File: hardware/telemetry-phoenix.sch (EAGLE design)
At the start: 111 parts, among them IC10 TPS70933, IC11 VN5160S-E, IC2 TPS70933, IC3 BME280, IC4 STM32L052C8T6, IC5 TPS62160, IC6 HX1, IC7 LMP7702, IC8 ADXL345, IC9 VN5160S-E, J1 GPS1, J2 RASPBERRYPI-GPIO, J3 POWER, J4 GPS2, J5 DNP, J6 SMA_EDGE, J9 IO, Q1 SI4202DY, Y1 32768, Y2 8M

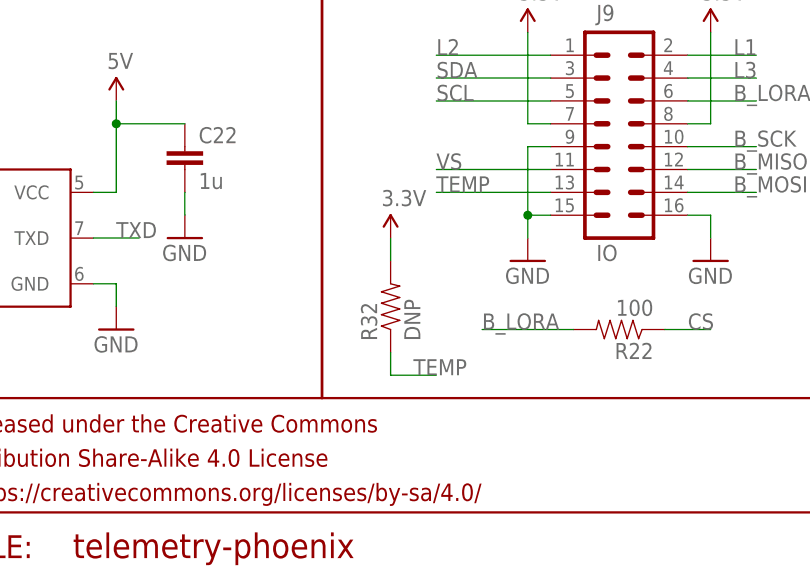
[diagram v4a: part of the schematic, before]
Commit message: Satisfy Adi on Phoenix power supply routing
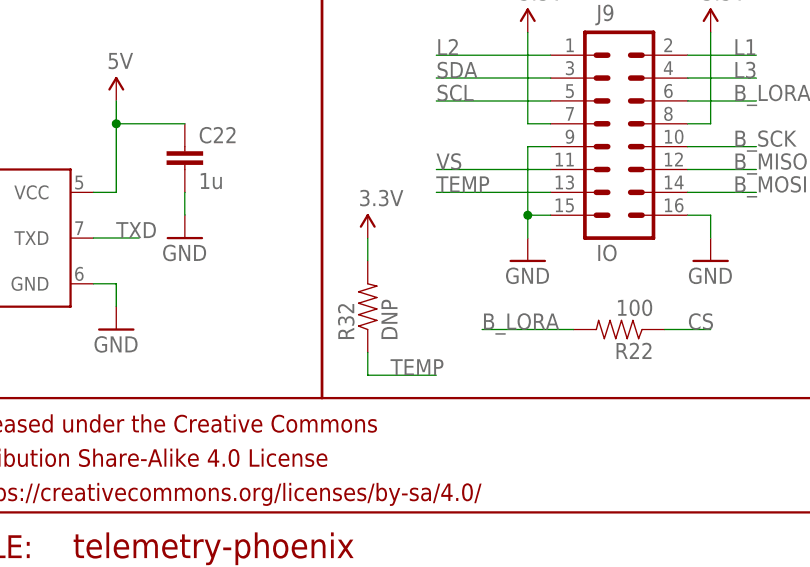
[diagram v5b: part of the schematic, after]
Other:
- moved on the sheet: R32
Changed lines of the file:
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@@
 <attribute name="VALUE" x="106.68" y="23.0886" size="1.778" layer="96"/>
 </instance>
-<instance part="R32" gate="G$1" x="198.12" y="45.72" rot="R90"/>
-<instance part="SUPPLY20" gate="G$1" x="198.12" y="53.34"/>
+<instance part="R32" gate="G$1" x="195.58" y="45.72" rot="R90"/>
+<instance part="SUPPLY20" gate="G$1" x="195.58" y="53.34"/>
 <instance part="R4" gate="G$1" x="368.3" y="137.16" rot="R180"/>
 <instance part="R25" gate="G$1" x="368.3" y="129.54" rot="R180"/>
@@
 <pinref part="R32" gate="G$1" pin="2"/>
 <pinref part="SUPPLY20" gate="G$1" pin="3.3V"/>
-<wire x1="198.12" y1="53.34" x2="198.12" y2="50.8" width="0.1524" layer="91"/>
+<wire x1="195.58" y1="53.34" x2="195.58" y2="50.8" width="0.1524" layer="91"/>
 </segment>
 <segment>
@@
 <segment>
 <pinref part="R32" gate="G$1" pin="1"/>
-<wire x1="198.12" y1="40.64" x2="198.12" y2="38.1" width="0.1524" layer="91"/>
-<wire x1="198.12" y1="38.1" x2="203.2" y2="38.1" width="0.1524" layer="91"/>
-<label x="200.66" y="38.1" size="1.778" layer="95"/>
-</segment>
-<segment>
+<wire x1="195.58" y1="40.64" x2="195.58" y2="38.1" width="0.1524" layer="91"/>
+<wire x1="195.58" y1="38.1" x2="203.2" y2="38.1" width="0.1524" layer="91"/>
+<label x="198.12" y="38.1" size="1.778" layer="95"/>
+</segment>
+<segment>

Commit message: Commit a few outstanding clean-up changes (not integrated into actual hardware) left in the current directory
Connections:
- net 3.3V: no longer R26.2
- net GND: now also R26.2
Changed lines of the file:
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@@
 <wire x1="45.72" y1="109.22" x2="45.72" y2="111.76" width="0.1524" layer="91"/>
 <junction x="45.72" y="111.76"/>
+<pinref part="R26" gate="G$1" pin="2"/>
+<wire x1="66.04" y1="109.22" x2="53.34" y2="109.22" width="0.1524" layer="91"/>
+<wire x1="53.34" y1="109.22" x2="53.34" y2="111.76" width="0.1524" layer="91"/>
+<junction x="53.34" y="111.76"/>
 </segment>
 <segment>
@@
 <pinref part="SUPPLY11" gate="G$1" pin="3.3V"/>
 <wire x1="73.66" y1="111.76" x2="73.66" y2="109.22" width="0.1524" layer="91"/>
-<wire x1="73.66" y1="109.22" x2="66.04" y2="109.22" width="0.1524" layer="91"/>
 <pinref part="R6" gate="G$1" pin="2"/>
-<junction x="73.66" y="109.22"/>
-<pinref part="R26" gate="G$1" pin="2"/>
-</segment>
-<segment>
+</segment>
+<segment>

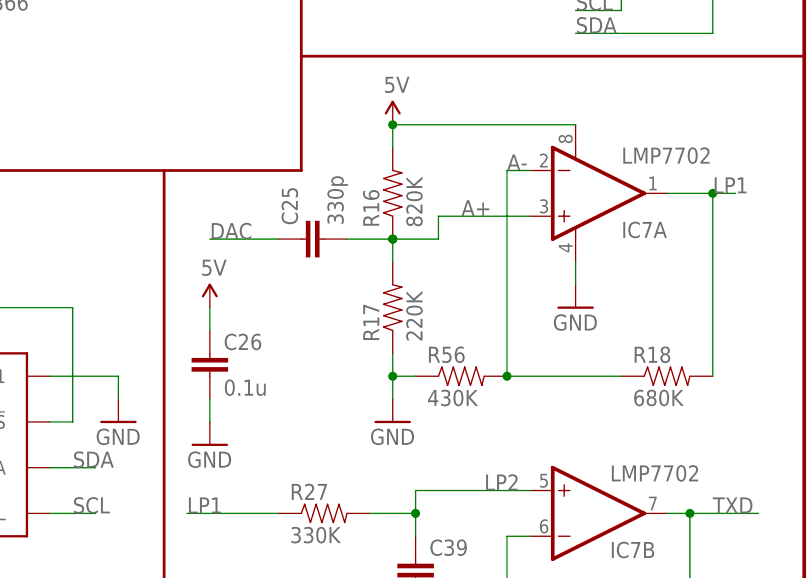
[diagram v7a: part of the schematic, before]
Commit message: Update schematic to hopefully fix phase angle issues with pre-emphasis filter
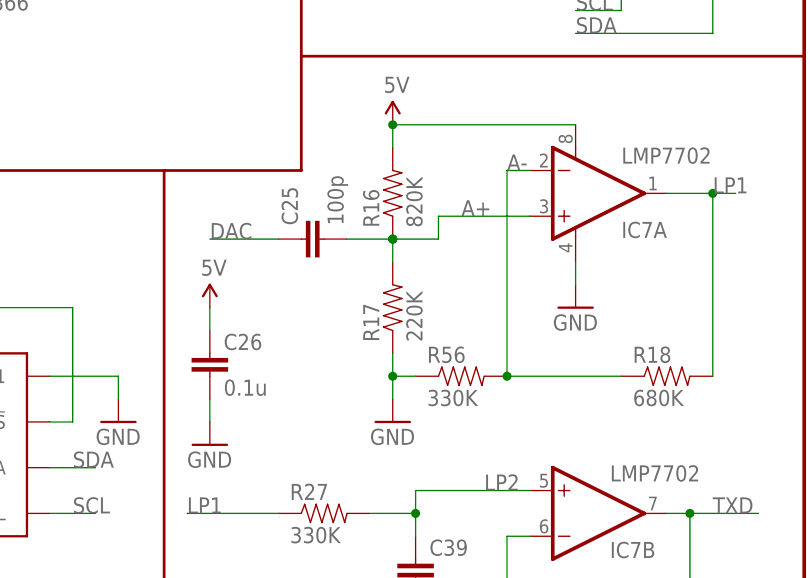
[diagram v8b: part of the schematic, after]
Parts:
- C25: value 330p -> 100p
- R56: value 430K -> 330K
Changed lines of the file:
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@@
 <part name="SUPPLY22" library="SparkFun-Aesthetics" deviceset="5V" device=""/>
 <part name="GND25" library="SparkFun-Aesthetics" deviceset="GND" device=""/>
-<part name="C25" library="SparkFun-Passives" deviceset="CAP" device="0805" value="330p"/>
+<part name="C25" library="SparkFun-Passives" deviceset="CAP" device="0805" value="100p"/>
 <part name="R16" library="SparkFun-Passives" deviceset="RESISTOR" device="0805-RES" value="820K"/>
 <part name="R17" library="SparkFun-Passives" deviceset="RESISTOR" device="0805-RES" value="220K"/>
@@
 <part name="GND40" library="SparkFun-Aesthetics" deviceset="GND" device=""/>
 <part name="GND48" library="SparkFun-Aesthetics" deviceset="GND" device=""/>
-<part name="R56" library="SparkFun-Passives" deviceset="RESISTOR" device="0805-RES" value="430K"/>
+<part name="R56" library="SparkFun-Passives" deviceset="RESISTOR" device="0805-RES" value="330K"/>
 <part name="SUPPLY25" library="SparkFun-Aesthetics" deviceset="5V" device=""/>
 <part name="R27" library="SparkFun-Passives" deviceset="RESISTOR" device="0805-RES" value="330K"/>
